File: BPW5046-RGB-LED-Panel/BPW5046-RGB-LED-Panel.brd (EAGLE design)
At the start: 24.9 x 40.6 mm, 3 parts, among them J1 COCOON_16BIT

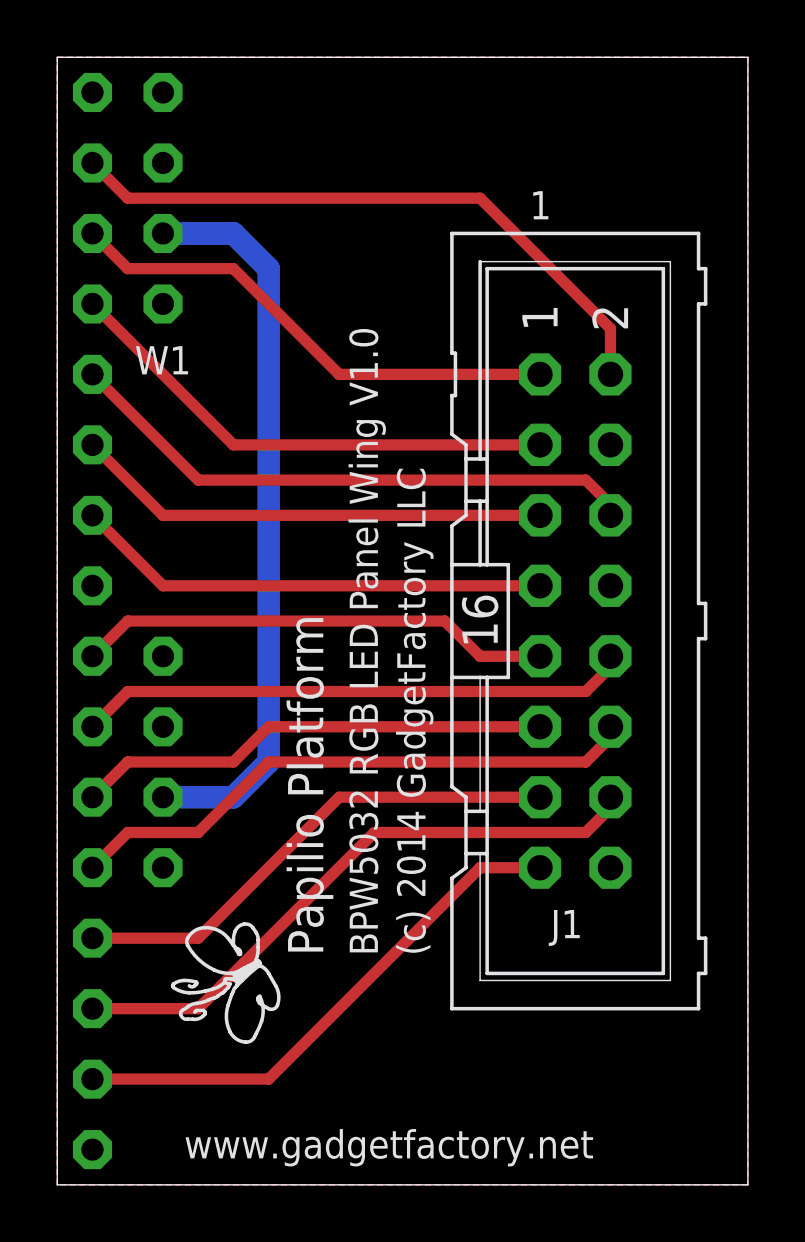
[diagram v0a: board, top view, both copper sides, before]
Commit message: RGB LED Panel
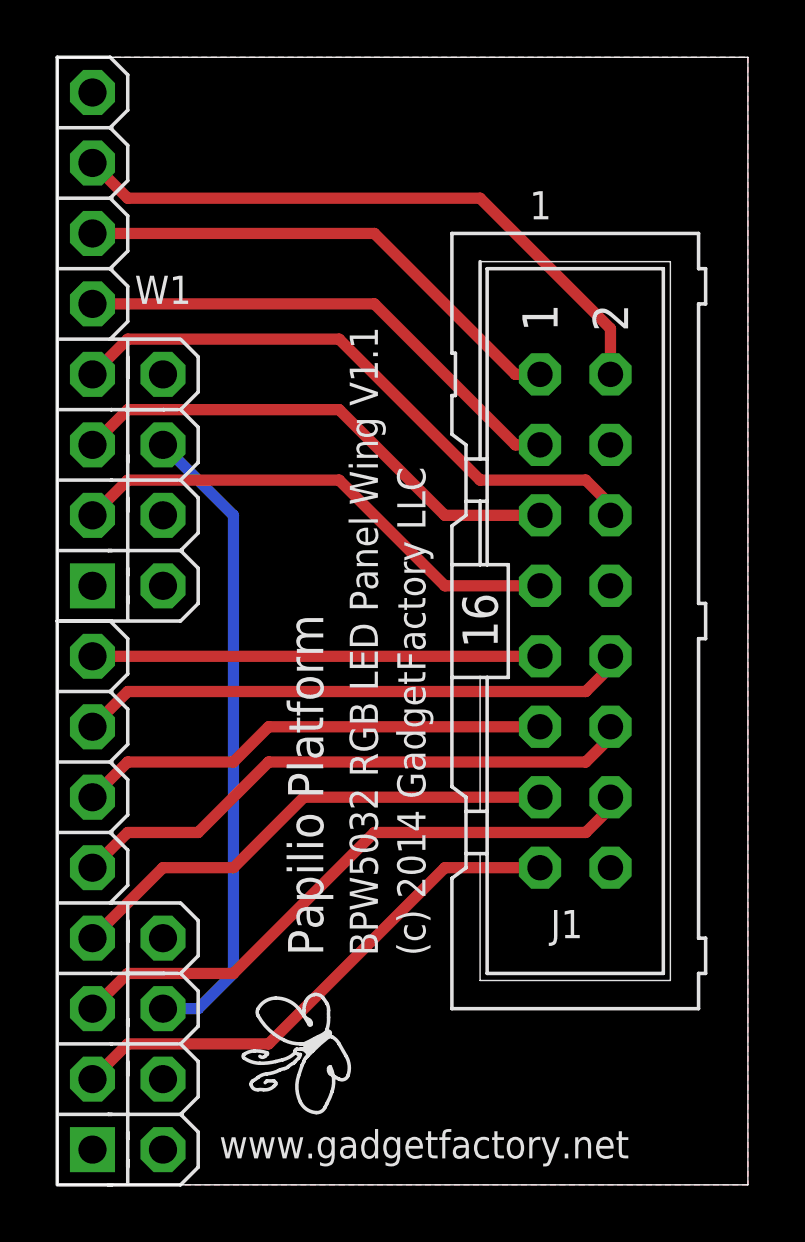
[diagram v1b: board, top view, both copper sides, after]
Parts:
- removed J1: COCOON_16BIT, usb1:COCOON_16BIT_LEFT
- added U$2, U$3: WING8WING8_NOHOLES, Papilio:WINGSIDE_8BIT_NOHOLES
- moved U$1 3.59 mm to (9.14, 4.83)
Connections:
- net 3V3: now also U$2.3V3@2, U$3.3V3@2; no longer J1.3V3W2@1, J1.3V3W2@2
- net A: now also U$3.7; no longer J1.A9@2
- net B: now also U$3.6; no longer J1.A10@2
- net B0: now also U$2.4; no longer J1.A4@2
- net B1: now also U$2.1; no longer J1.A7@2
- net C: now also U$3.5; no longer J1.A11@2
- net CLK: now also U$3.3; no longer J1.A13@2
- net D: now also U$3.4; no longer J1.A12@2
- net G0: now also U$2.6; no longer J1.A2@2
- net G1: now also U$2.3; no longer J1.A5@2
- net GND: now also U$2.GND@2, U$3.GND@2; no longer J1.GNDW2@1, J1.GNDW2@2
- net OE: now also U$3.1; no longer J1.A15@2
- net R0: now also U$2.5; no longer J1.A3@2
- net R1: now also U$2.2; no longer J1.A6@2
- net STB: now also U$3.2; no longer J1.A14@2
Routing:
- net 3V3: track 26.5 -> 23.2 mm
- net R1: track 17.2 -> 18.2 mm
- net G1: track 21.0 -> 22.0 mm
- net B1: track 17.2 -> 18.2 mm
- net A: track 17.2 -> 16.1 mm
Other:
- board text added: "BPW5032 RGB LED Panel Wing V1.1"
- board text removed: "BPW5032 RGB LED Panel Wing V1.0"
